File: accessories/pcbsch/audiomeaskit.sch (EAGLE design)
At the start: 27 parts, among them IC25 INA331IDGK

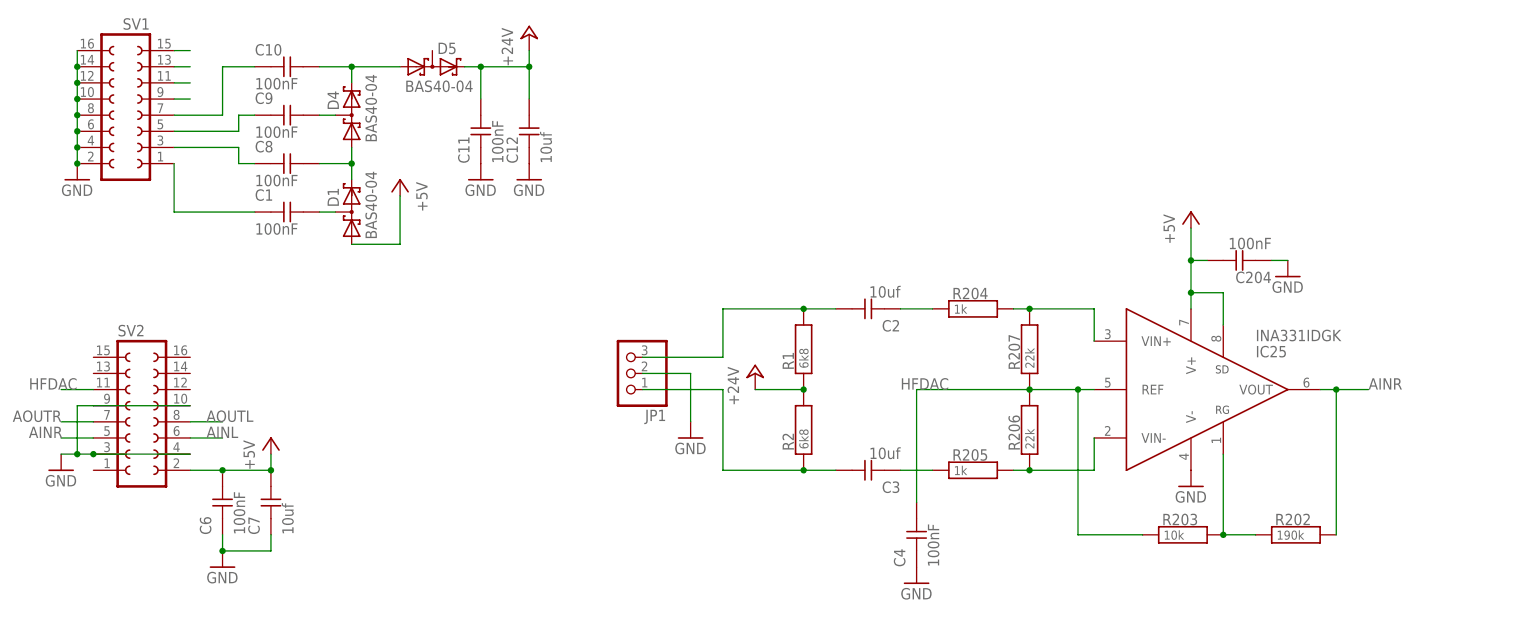
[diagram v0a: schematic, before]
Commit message: added sync on fpga and fix some things on audiomeaskit
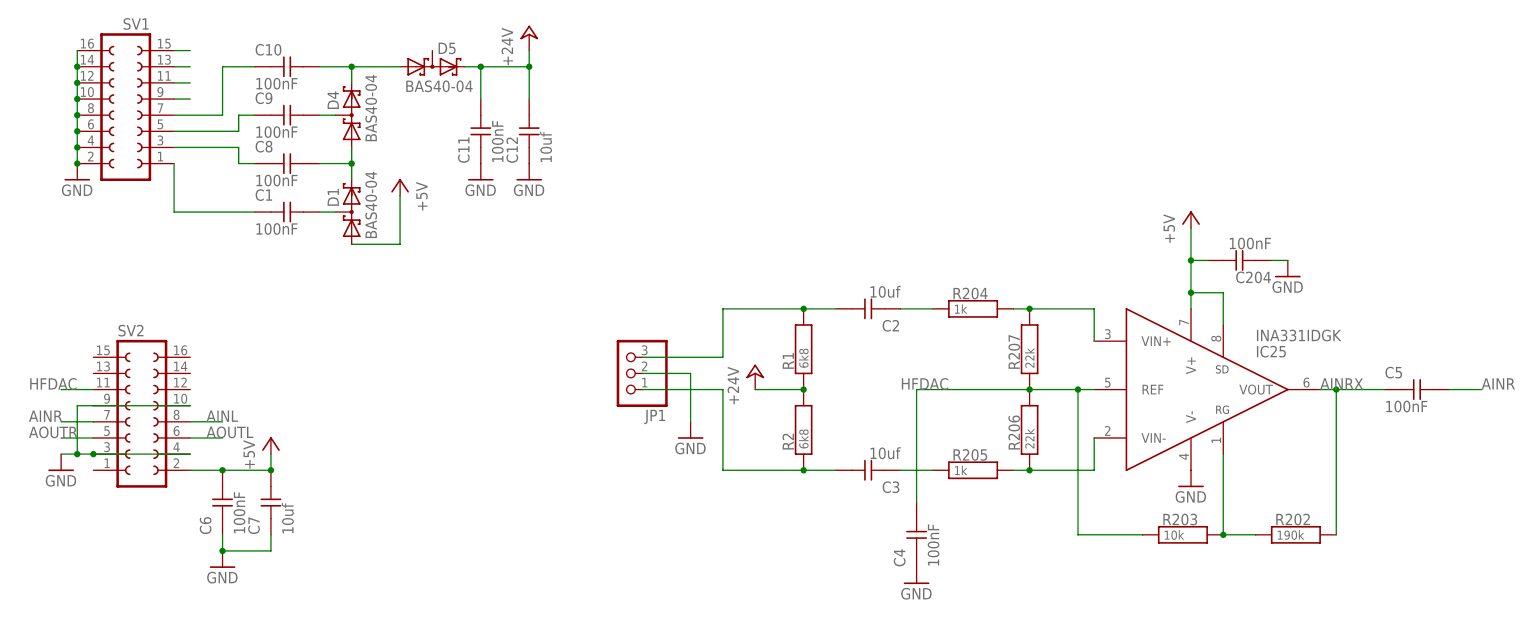
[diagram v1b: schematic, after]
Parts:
- added C5: 100nF, passive:CAPC0603
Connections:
- new net AINRX: C5.1, IC25.VOUT, R202.P$2
- net AINL: now also SV2.8; no longer SV2.6
- net AINR: now also C5.2, SV2.7; no longer IC25.VOUT, R202.P$2, SV2.5
- net AOUTL: now also SV2.6; no longer SV2.8
- net AOUTR: now also SV2.5; no longer SV2.7
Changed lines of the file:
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@@
 <grid distance="0.1" unitdist="inch" unit="inch" style="lines" multiple="1" display="no" altdistance="0.01" altunitdist="inch" altunit="inch"/>
 <layers>
-<layer number="1" name="Top" color="4" fill="1" visible="yes" active="no"/>
-<layer number="2" name="Route2" color="1" fill="3" visible="yes" active="no"/>
-<layer number="3" name="Route3" color="4" fill="3" visible="yes" active="no"/>
-<layer number="14" name="Route14" color="1" fill="6" visible="yes" active="no"/>
-<layer number="15" name="Route15" color="4" fill="6" visible="yes" active="no"/>
-<layer number="16" name="Bottom" color="1" fill="1" visible="yes" active="no"/>
-<layer number="17" name="Pads" color="2" fill="1" visible="yes" active="no"/>
-<layer number="18" name="Vias" color="2" fill="1" visible="yes" active="no"/>
-<layer number="19" name="Unrouted" color="6" fill="1" visible="yes" active="no"/>
-<layer number="20" name="Dimension" color="15" fill="1" visible="yes" active="no"/>
-<layer number="21" name="tPlace" color="7" fill="1" visible="yes" active="no"/>
-<layer number="22" name="bPlace" color="7" fill="1" visible="yes" active="no"/>
-<layer number="23" name="tOrigins" color="15" fill="1" visible="yes" active="no"/>
-<layer number="24" name="bOrigins" color="15" fill="1" visible="yes" active="no"/>
-<layer number="25" name="tNames" color="7" fill="1" visible="yes" active="no"/>
-<layer number="26" name="bNames" color="7" fill="1" visible="yes" active="no"/>
-<layer number="27" name="tValues" color="7" fill="1" visible="yes" active="no"/>
-<layer number="28" name="bValues" color="7" fill="1" visible="yes" active="no"/>
+<layer number="1" name="Top" color="4" fill="1" visible="no" active="no"/>
+<layer number="2" name="Route2" color="1" fill="3" visible="no" active="no"/>
+<layer number="3" name="Route3" color="4" fill="3" visible="no" active="no"/>
+<layer number="14" name="Route14" color="1" fill="6" visible="no" active="no"/>
+<layer number="15" name="Route15" color="4" fill="6" visible="no" active="no"/>
+<layer number="16" name="Bottom" color="1" fill="1" visible="no" active="no"/>
+<layer number="17" name="Pads" color="2" fill="1" visible="no" active="no"/>
+<layer number="18" name="Vias" color="2" fill="1" visible="no" active="no"/>
+<layer number="19" name="Unrouted" color="6" fill="1" visible="no" active="no"/>
+<layer number="20" name="Dimension" color="15" fill="1" visible="no" active="no"/>
+<layer number="21" name="tPlace" color="7" fill="1" visible="no" active="no"/>
+<layer number="22" name="bPlace" color="7" fill="1" visible="no" active="no"/>
+<layer number="23" name="tOrigins" color="15" fill="1" visible="no" active="no"/>
+<layer number="24" name="bOrigins" color="15" fill="1" visible="no" active="no"/>
+<layer number="25" name="tNames" color="7" fill="1" visible="no" active="no"/>
+<layer number="26" name="bNames" color="7" fill="1" visible="no" active="no"/>
+<layer number="27" name="tValues" color="7" fill="1" visible="no" active="no"/>
+<layer number="28" name="bValues" color="7" fill="1" visible="no" active="no"/>
 <layer number="29" name="tStop" color="7" fill="3" visible="no" active="no"/>
 <layer number="30" name="bStop" color="7" fill="6" visible="no" active="no"/>
@@
 <layer number="35" name="tGlue" color="7" fill="4" visible="no" active="no"/>
 <layer number="36" name="bGlue" color="7" fill="5" visible="no" active="no"/>
-<layer number="37" name="tTest" color="7" fill="1" visible="yes" active="no"/>
-<layer number="38" name="bTest" color="7" fill="1" visible="yes" active="no"/>
+<layer number="37" name="tTest" color="7" fill="1" visible="no" active="no"/>
+<layer number="38" name="bTest" color="7" fill="1" visible="no" active="no"/>
 <layer number="39" name="tKeepout" color="4" fill="11" visible="no" active="no"/>
 <layer number="40" name="bKeepout" color="1" fill="11" visible="no" active="no"/>
@@
 <layer number="44" name="Drills" color="7" fill="1" visible="no" active="no"/>
 <layer number="45" name="Holes" color="7" fill="1" visible="no" active="no"/>
-<layer number="46" name="Milling" color="3" fill="1" visible="yes" active="no"/>
-<layer number="47" name="Measures" color="7" fill="1" visible="yes" active="no"/>
-<layer number="48" name="Document" color="7" fill="1" visible="yes" active="no"/>
-<layer number="49" name="Reference" color="7" fill="1" visible="yes" active="no"/>
-<layer number="50" name="dxf" color="7" fill="1" visible="yes" active="no"/>
-<layer number="51" name="tDocu" color="7" fill="1" visible="yes" active="no"/>
-<layer number="52" name="bDocu" color="7" fill="1" visible="yes" active="no"/>
-<layer number="53" name="tGND_GNDA" color="7" fill="1" visible="yes" active="no"/>
-<layer number="54" name="bGND_GNDA" color="7" fill="1" visible="yes" active="no"/>
+<layer number="46" name="Milling" color="3" fill="1" visible="no" active="no"/>
+<layer number="47" name="Measures" color="7" fill="1" visible="no" active="no"/>
+<layer number="48" name="Document" color="7" fill="1" visible="no" active="no"/>
+<layer number="49" name="Reference" color="7" fill="1" visible="no" active="no"/>
+<layer number="50" name="dxf" color="7" fill="1" visible="no" active="no"/>
+<layer number="51" name="tDocu" color="7" fill="1" visible="no" active="no"/>
+<layer number="52" name="bDocu" color="7" fill="1" visible="no" active="no"/>
+<layer number="53" name="tGND_GNDA" color="7" fill="1" visible="no" active="no"/>
+<layer number="54" name="bGND_GNDA" color="7" fill="1" visible="no" active="no"/>
 <layer number="90" name="Modules" color="5" fill="1" visible="yes" active="yes"/>
 <layer number="91" name="Nets" color="2" fill="1" visible="yes" active="yes"/>
@@
 <part name="GND2" library="supply1" deviceset="GND" device=""/>
 <part name="GND7" library="supply1" deviceset="GND" device=""/>
+<part name="C5" library="passive" deviceset="CAP" device="C0603" value="100nF"/>
 </parts>
 <sheets>
@@
 <instance part="GND2" gate="1" x="-45.72" y="22.86"/>
 <instance part="GND7" gate="1" x="-43.18" y="68.58"/>
+<instance part="C5" gate="G$1" x="167.64" y="35.56"/>
 </instances>
 <busses>
@@
 <net name="AINR" class="0">
 <segment>
-<pinref part="R202" gate="G$1" pin="P$2"/>
-<wire x1="154.94" y1="12.7" x2="154.94" y2="35.56" width="0.1524" layer="91"/>
-<pinref part="IC25" gate="G$1" pin="VOUT"/>
-<wire x1="154.94" y1="35.56" x2="152.4" y2="35.56" width="0.1524" layer="91"/>
-<wire x1="154.94" y1="35.56" x2="160.02" y2="35.56" width="0.1524" layer="91"/>
-<label x="160.02" y="35.56" size="1.778" layer="95"/>
-<junction x="154.94" y="35.56"/>
-</segment>
-<segment>
-<pinref part="SV2" gate="G$1" pin="5"/>
-<wire x1="-40.64" y1="27.94" x2="-45.72" y2="27.94" width="0.1524" layer="91"/>
-<label x="-50.8" y="27.94" size="1.778" layer="95"/>
+<pinref part="SV2" gate="G$1" pin="7"/>
+<wire x1="-40.64" y1="30.48" x2="-45.72" y2="30.48" width="0.1524" layer="91"/>
+<label x="-50.8" y="30.48" size="1.778" layer="95"/>
+</segment>
+<segment>
+<pinref part="C5" gate="G$1" pin="2"/>
+<wire x1="172.72" y1="35.56" x2="177.8" y2="35.56" width="0.1524" layer="91"/>
+<label x="177.8" y="35.56" size="1.778" layer="95"/>
 </segment>
 </net>
@@
 </segment>
 </net>
-<net name="AOUTL" class="0">
+<net name="AOUTR" class="0">
+<segment>
+<pinref part="SV2" gate="G$1" pin="5"/>
+<wire x1="-40.64" y1="27.94" x2="-45.72" y2="27.94" width="0.1524" layer="91"/>
+<label x="-50.8" y="27.94" size="1.778" layer="95"/>
+</segment>
+</net>
+<net name="AINL" class="0">
 <segment>
 <pinref part="SV2" gate="G$1" pin="8"/>
@@
 </segment>
 </net>
-<net name="AOUTR" class="0">
-<segment>
-<pinref part="SV2" gate="G$1" pin="7"/>
-<wire x1="-40.64" y1="30.48" x2="-45.72" y2="30.48" width="0.1524" layer="91"/>
-<label x="-53.34" y="30.48" size="1.778" layer="95"/>
-</segment>
-</net>
-<net name="AINL" class="0">
+<net name="S1" class="0">
+<segment>
+<pinref part="SV1" gate="G$1" pin="9"/>
+<wire x1="-27.94" y1="81.28" x2="-25.4" y2="81.28" width="0.1524" layer="91"/>
+</segment>
+</net>
+<net name="S2" class="0">
+<segment>
+<pinref part="SV1" gate="G$1" pin="11"/>
+<wire x1="-27.94" y1="83.82" x2="-25.4" y2="83.82" width="0.1524" layer="91"/>
+</segment>
+</net>
+<net name="S3" class="0">
+<segment>
+<pinref part="SV1" gate="G$1" pin="13"/>
+<wire x1="-27.94" y1="86.36" x2="-25.4" y2="86.36" width="0.1524" layer="91"/>
+</segment>
+</net>
+<net name="S4" class="0">
+<segment>
+<pinref part="SV1" gate="G$1" pin="15"/>
+<wire x1="-27.94" y1="88.9" x2="-25.4" y2="88.9" width="0.1524" layer="91"/>
+</segment>
+</net>
+<net name="AOUTL" class="0">
 <segment>
 <pinref part="SV2" gate="G$1" pin="6"/>
@@
 </segment>
 </net>
-<net name="S1" class="0">
-<segment>
-<pinref part="SV1" gate="G$1" pin="9"/>
-<wire x1="-27.94" y1="81.28" x2="-25.4" y2="81.28" width="0.1524" layer="91"/>
-</segment>
-</net>
-<net name="S2" class="0">
-<segment>
-<pinref part="SV1" gate="G$1" pin="11"/>
-<wire x1="-27.94" y1="83.82" x2="-25.4" y2="83.82" width="0.1524" layer="91"/>
-</segment>
-</net>
-<net name="S3" class="0">
-<segment>
-<pinref part="SV1" gate="G$1" pin="13"/>
-<wire x1="-27.94" y1="86.36" x2="-25.4" y2="86.36" width="0.1524" layer="91"/>
-</segment>
-</net>
-<net name="S4" class="0">
-<segment>
-<pinref part="SV1" gate="G$1" pin="15"/>
-<wire x1="-27.94" y1="88.9" x2="-25.4" y2="88.9" width="0.1524" layer="91"/>
-</segment>
-</net>
+<net name="AINRX" class="0">
+<segment>
+<pinref part="R202" gate="G$1" pin="P$2"/>
+<wire x1="154.94" y1="12.7" x2="154.94" y2="35.56" width="0.1524" layer="91"/>
+<pinref part="IC25" gate="G$1" pin="VOUT"/>
+<wire x1="154.94" y1="35.56" x2="152.4" y2="35.56" width="0.1524" layer="91"/>
+<label x="152.4" y="35.56" size="1.778" layer="95"/>
+<pinref part="C5" gate="G$1" pin="1"/>
+<wire x1="154.94" y1="35.56" x2="162.56" y2="35.56" width="0.1524" layer="91"/>
+<junction x="154.94" y="35.56"/>
+</segment>
+</net>
